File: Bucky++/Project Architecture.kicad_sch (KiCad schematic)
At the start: 0 parts

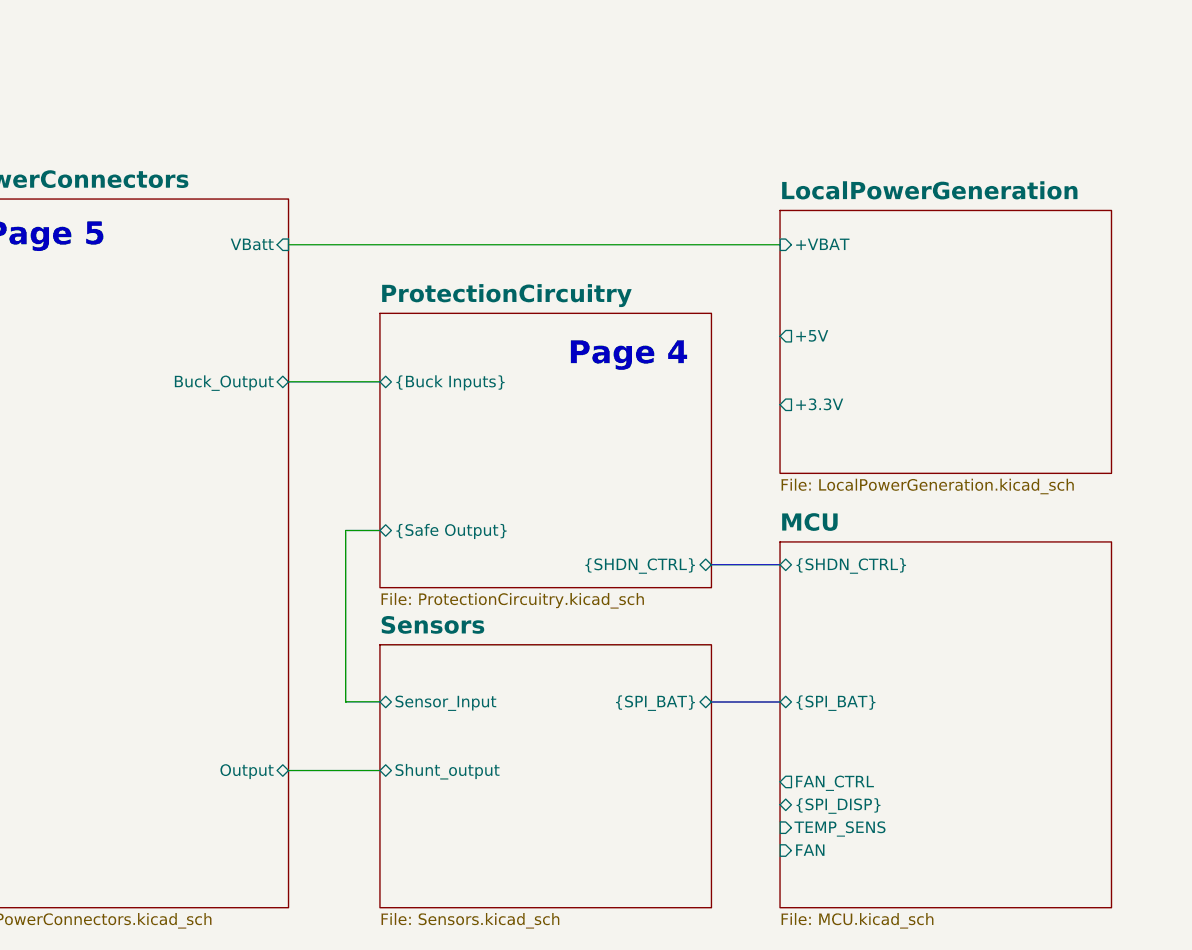
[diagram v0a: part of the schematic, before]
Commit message: added over-current protection on main input
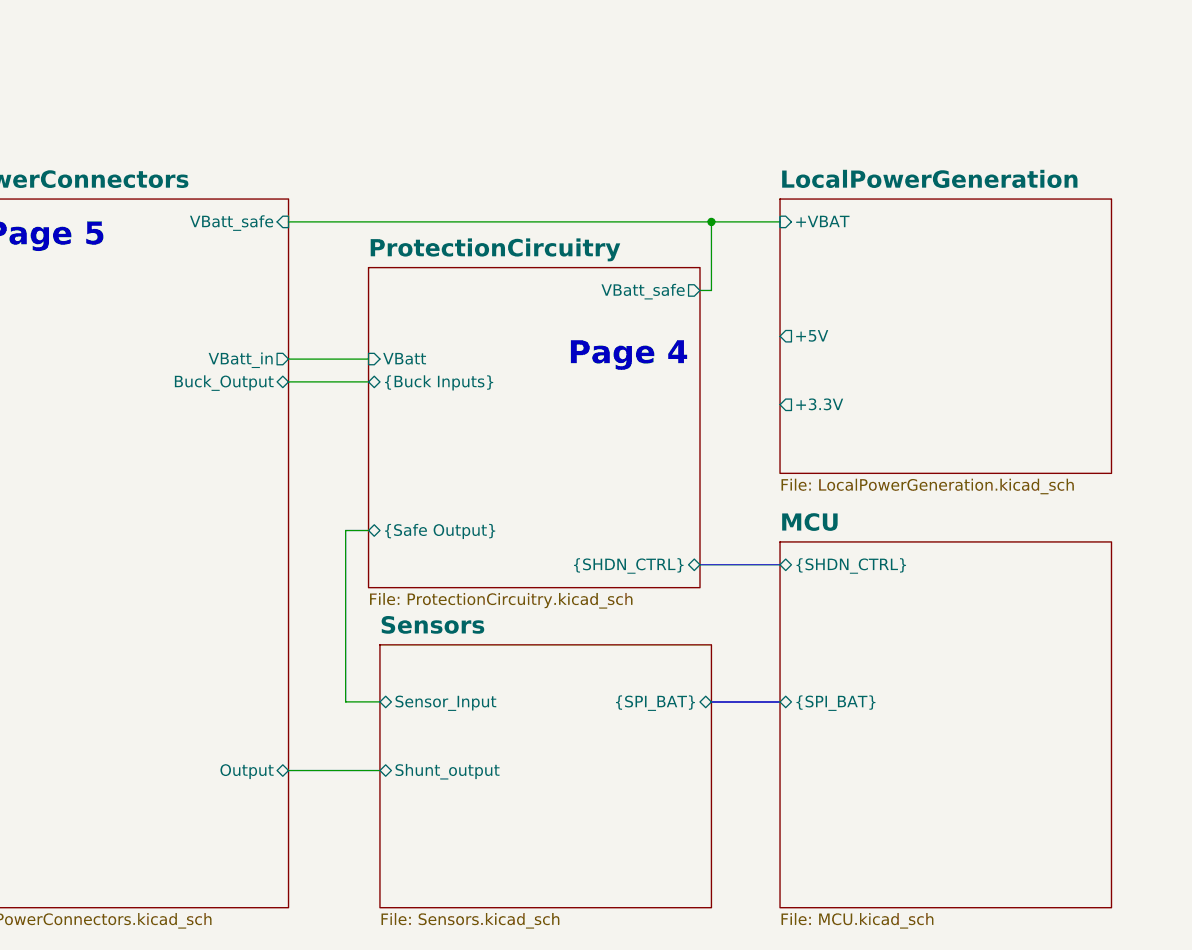
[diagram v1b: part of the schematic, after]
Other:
- sheet MCU ports: added none; removed FAN, FAN_CTRL, TEMP_SENS, {SPI_DISP}
- sheet PowerConnectors ports: added VBatt_in, VBatt_safe; removed VBatt
- sheet ProtectionCircuitry ports: added VBatt, VBatt_safe; removed none
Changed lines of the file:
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@@
 		)
 	)
-	(wire
-		(pts
-			(xy 124.46 99.06) (xy 128.27 99.06)
+	(junction
+		(at 165.1 64.77)
+		(diameter 0)
+		(color 0 0 0 0)
+	)
+	(wire
+		(pts
+			(xy 163.83 72.39) (xy 165.1 72.39)
+		)
+		(stroke
+			(width 0)
+			(type default)
+		)
+	)
+	(wire
+		(pts
+			(xy 124.46 99.06) (xy 127 99.06)
+		)
+		(stroke
+			(width 0)
+			(type default)
+		)
+	)
+	(wire
+		(pts
+			(xy 118.11 64.77) (xy 165.1 64.77)
 		)
 		(stroke
@@
 	(wire
 		(pts
-			(xy 118.11 82.55) (xy 128.27 82.55)
+			(xy 118.11 82.55) (xy 127 82.55)
+		)
+		(stroke
+			(width 0)
+			(type default)
+		)
+	)
+	(wire
+		(pts
+			(xy 118.11 80.01) (xy 127 80.01)
+		)
+		(stroke
+			(width 0)
+			(type default)
+		)
+	)
+	(wire
+		(pts
+			(xy 165.1 64.77) (xy 172.72 64.77)
 		)
 		(stroke
@@
 		)
 	)
+	(wire
+		(pts
+			(xy 165.1 64.77) (xy 165.1 72.39)
+		)
+		(stroke
+			(width 0)
+			(type default)
+		)
+	)
 	(bus
 		(pts
-			(xy 165.1 102.87) (xy 172.72 102.87)
+			(xy 163.83 102.87) (xy 172.72 102.87)
 		)
 		(stroke
@@
 		(pts
 			(xy 124.46 118.11) (xy 124.46 99.06)
-		)
-		(stroke
-			(width 0)
-			(type default)
-		)
-	)
-	(wire
-		(pts
-			(xy 118.11 67.31) (xy 172.72 67.31)
 		)
 		(stroke
@@
 			)
 		)
-		(pin "VBatt" input
-			(at 118.11 67.31 0)
-			(effects
-				(font
-					(size 1.27 1.27)
-				)
-				(justify right)
-			)
-		)
 		(pin "Buck_Output" tri_state
 			(at 118.11 82.55 0)
@@
 		(pin "Output" tri_state
 			(at 118.11 125.73 0)
+			(effects
+				(font
+					(size 1.27 1.27)
+				)
+				(justify right)
+			)
+		)
+		(pin "VBatt_safe" input
+			(at 118.11 64.77 0)
+			(effects
+				(font
+					(size 1.27 1.27)
+				)
+				(justify right)
+			)
+		)
+		(pin "VBatt_in" output
+			(at 118.11 80.01 0)
 			(effects
 				(font
@@
 	)
 	(sheet
-		(at 172.72 63.5)
-		(size 36.83 29.21)
+		(at 172.72 62.23)
+		(size 36.83 30.48)
 		(exclude_from_sim no)
 		(in_bom yes)
@@
 		)
 		(property "Sheetname" "LocalPowerGeneration"
-			(at 172.72 62.4709 0)
+			(at 172.72 61.2009 0)
 			(effects
 				(font
@@
 		)
 		(pin "+VBAT" input
-			(at 172.72 67.31 180)
+			(at 172.72 64.77 180)
 			(effects
 				(font
@@
 			)
 		)
-		(pin "FAN" input
-			(at 172.72 134.62 180)
-			(effects
-				(font
-					(size 1.27 1.27)
-				)
-				(justify left)
-			)
-		)
-		(pin "TEMP_SENS" input
-			(at 172.72 132.08 180)
-			(effects
-				(font
-					(size 1.27 1.27)
-				)
-				(justify left)
-			)
-		)
-		(pin "{SPI_DISP}" bidirectional
-			(at 172.72 129.54 180)
-			(effects
-				(font
-					(size 1.27 1.27)
-				)
-				(justify left)
-			)
-		)
 		(pin "{SHDN_CTRL}" bidirectional
 			(at 172.72 102.87 180)
@@
 		(pin "{SPI_BAT}" bidirectional
 			(at 172.72 118.11 180)
-			(effects
-				(font
-					(size 1.27 1.27)
-				)
-				(justify left)
-			)
-		)
-		(pin "FAN_CTRL" output
-			(at 172.72 127 180)
 			(effects
 				(font
@@
 	)
 	(sheet
-		(at 128.27 74.93)
-		(size 36.83 30.48)
+		(at 127 69.85)
+		(size 36.83 35.56)
 		(exclude_from_sim no)
 		(in_bom yes)
@@
 		)
 		(property "Sheetname" "ProtectionCircuitry"
-			(at 128.27 73.9009 0)
+			(at 127 68.8209 0)
 			(effects
 				(font
@@
 		)
 		(property "Sheetfile" "ProtectionCircuitry.kicad_sch"
-			(at 128.27 105.9946 0)
+			(at 127 105.9946 0)
 			(effects
 				(font
@@
 		)
 		(pin "{Buck Inputs}" tri_state
-			(at 128.27 82.55 180)
+			(at 127 82.55 180)
 			(effects
 				(font
@@
 		)
 		(pin "{Safe Output}" tri_state
-			(at 128.27 99.06 180)
+			(at 127 99.06 180)
 			(effects
 				(font
@@
 		)
 		(pin "{SHDN_CTRL}" tri_state
-			(at 165.1 102.87 0)
-			(effects
-				(font
+			(at 163.83 102.87 0)
+			(effects
+				(font
+					(size 1.27 1.27)
+				)
+				(justify right)
+			)
+		)
+		(pin "VBatt" input
+			(at 127 80.01 180)
+			(effects
+				(font
+					(size 1.27 1.27)
+				)
+				(justify left)
+			)
+		)
+		(pin "VBatt_safe" output
+			(at 163.83 72.39 0)
+			(effects
+				(font

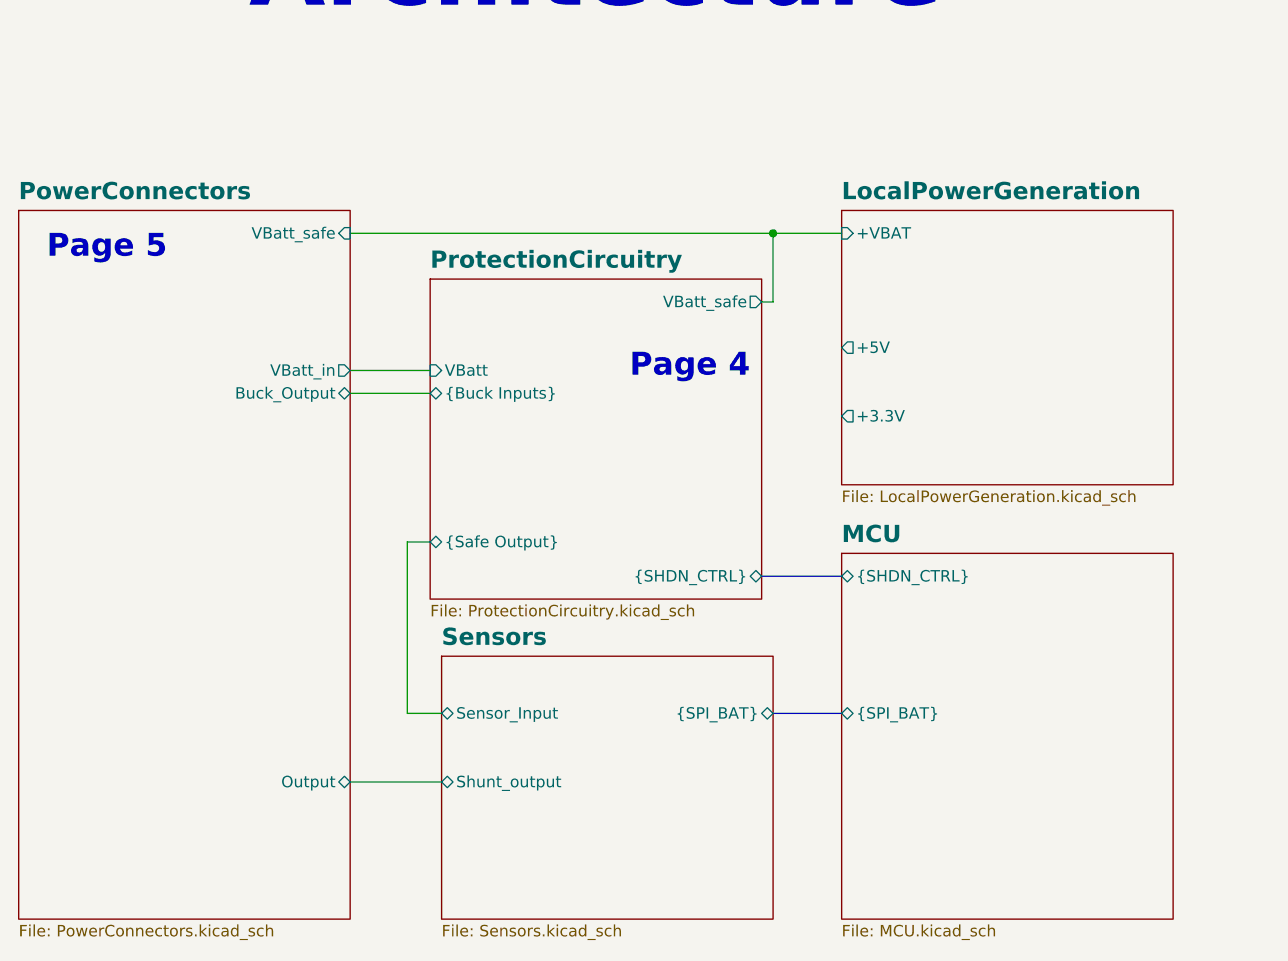
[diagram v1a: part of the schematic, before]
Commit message: fixed errors and added protection diodes
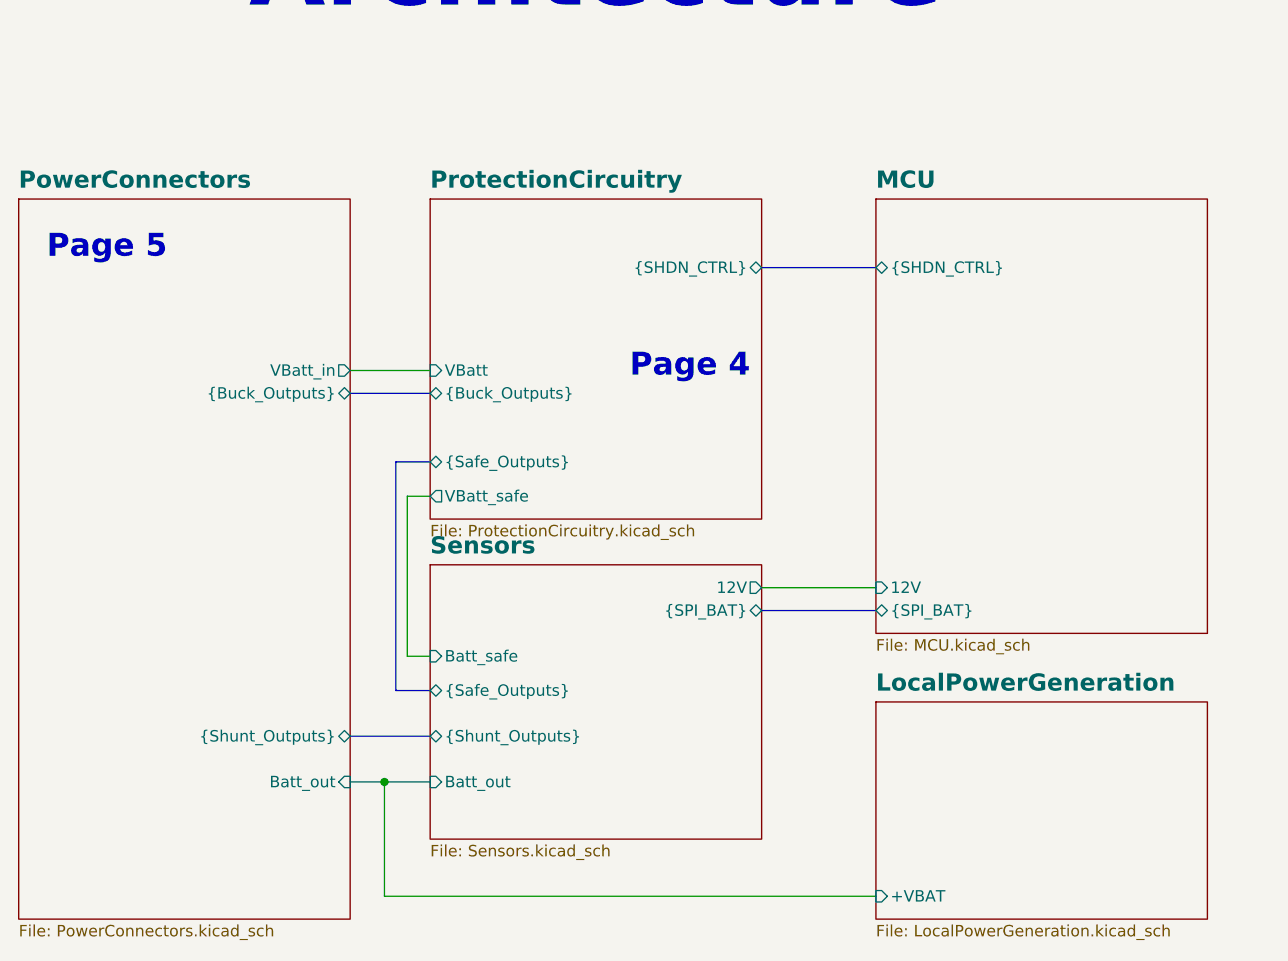
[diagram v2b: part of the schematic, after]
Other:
- sheet LocalPowerGeneration ports: added none; removed +3.3V, +5V
- sheet MCU ports: added 12V; removed none
- sheet PowerConnectors ports: added Batt_out, {Buck_Outputs}, {Shunt_Outputs}; removed Buck_Output, Output, VBatt_safe
- sheet ProtectionCircuitry ports: added {Buck_Outputs}, {Safe_Outputs}; removed {Buck Inputs}, {Safe Output}
- sheet Sensors ports: added 12V, Batt_out, Batt_safe, {Safe_Outputs}, {Shunt_Outputs}; removed Sensor_Input, Shunt_output

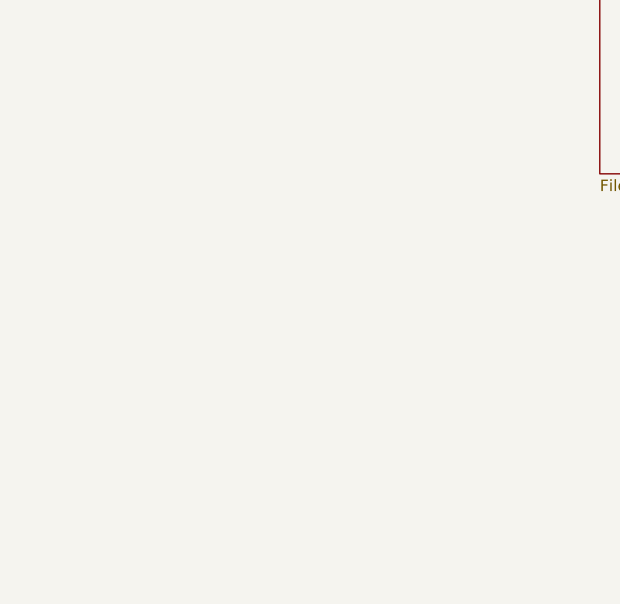
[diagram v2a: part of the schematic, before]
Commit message: initial component placement
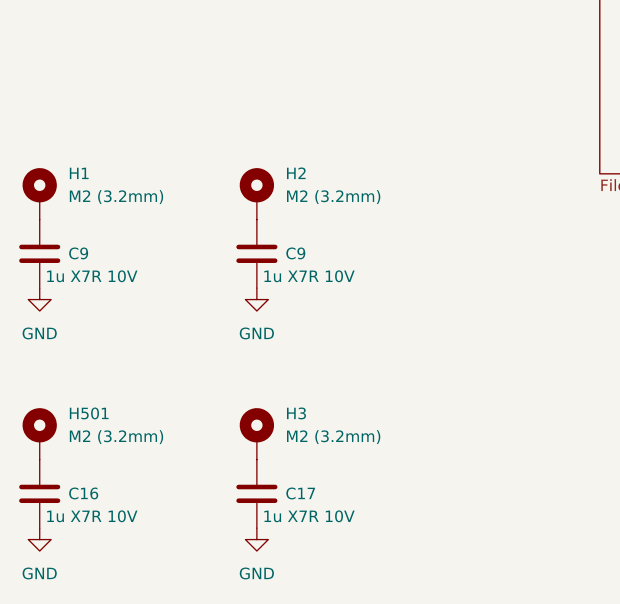
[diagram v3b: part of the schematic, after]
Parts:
- added C16, C17, C9 (x2): 1u X7R 10V, 0_capacitor_smd:C_0402_1005_DensityHigh, symbol Device:C
- added H1, H2, H3, H501: M2 (3.2mm), MountingHole:MountingHole_2.2mm_M2_Pad_Via, symbol Mechanical:MountingHole_Pad
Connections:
- new net: C9.1, H2.1
- new net: C17.1, H3.1
- new net: C9.1, H1.1
- new net: C16.1, H501.1
- new net GND: C16.2, C17.2, C9.2, C9.2

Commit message: worked on layout, added adm1270
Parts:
- renumbered C9 to C17, C17 to C21
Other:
- sheet PowerConnectors ports: added {Safe_Outputs}; removed {Shunt_Outputs}
- sheet ProtectionCircuitry ports: added 12V_fans, VBatt_protection, {Shunt_Outputs}; removed VBatt, {Buck_Outputs}
- sheet Sensors ports: added Batt_in, Batt_protection, {Buck_Outputs}; removed 12V, Batt_out, Batt_safe, {Safe_Outputs}
